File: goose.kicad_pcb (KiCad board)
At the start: 2 copper layers, 28 x 28 mm, 9 parts, among them J1 Conn_01x04, U1 AT42QT1011-TSHR

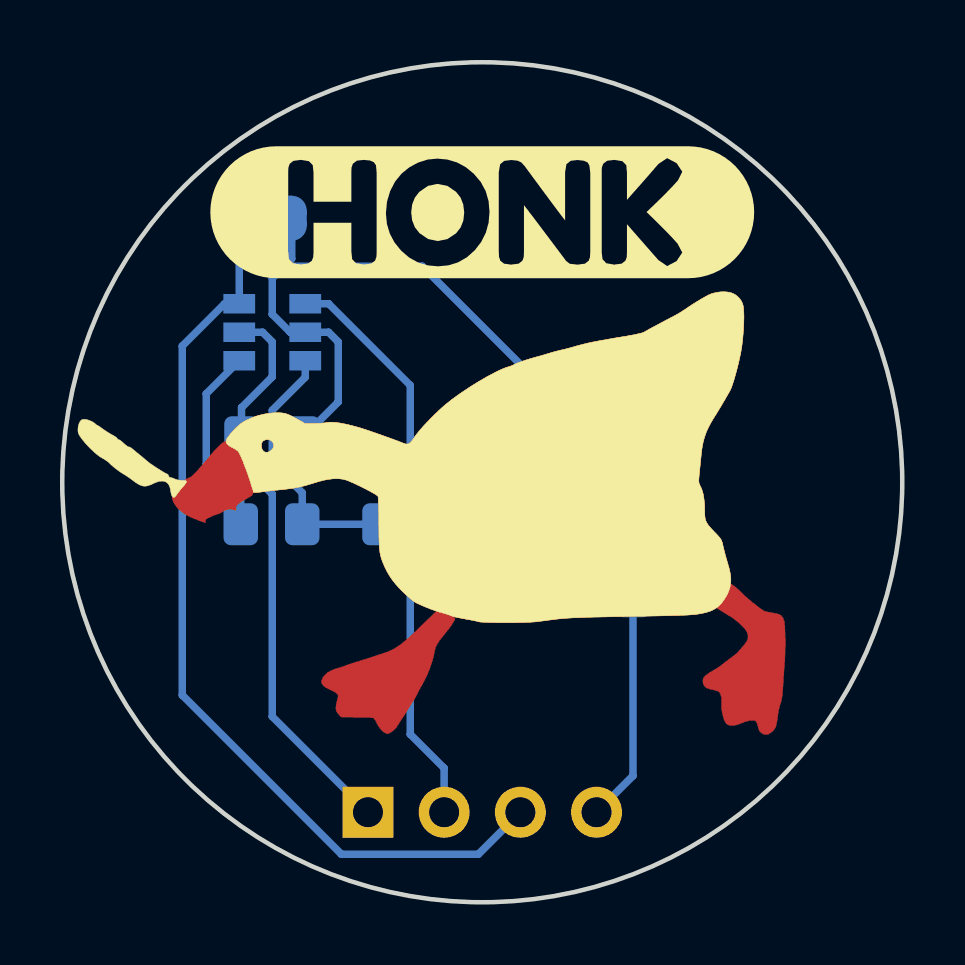
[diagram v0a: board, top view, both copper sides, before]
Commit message: Added a version that uses a chip that's actually in stock
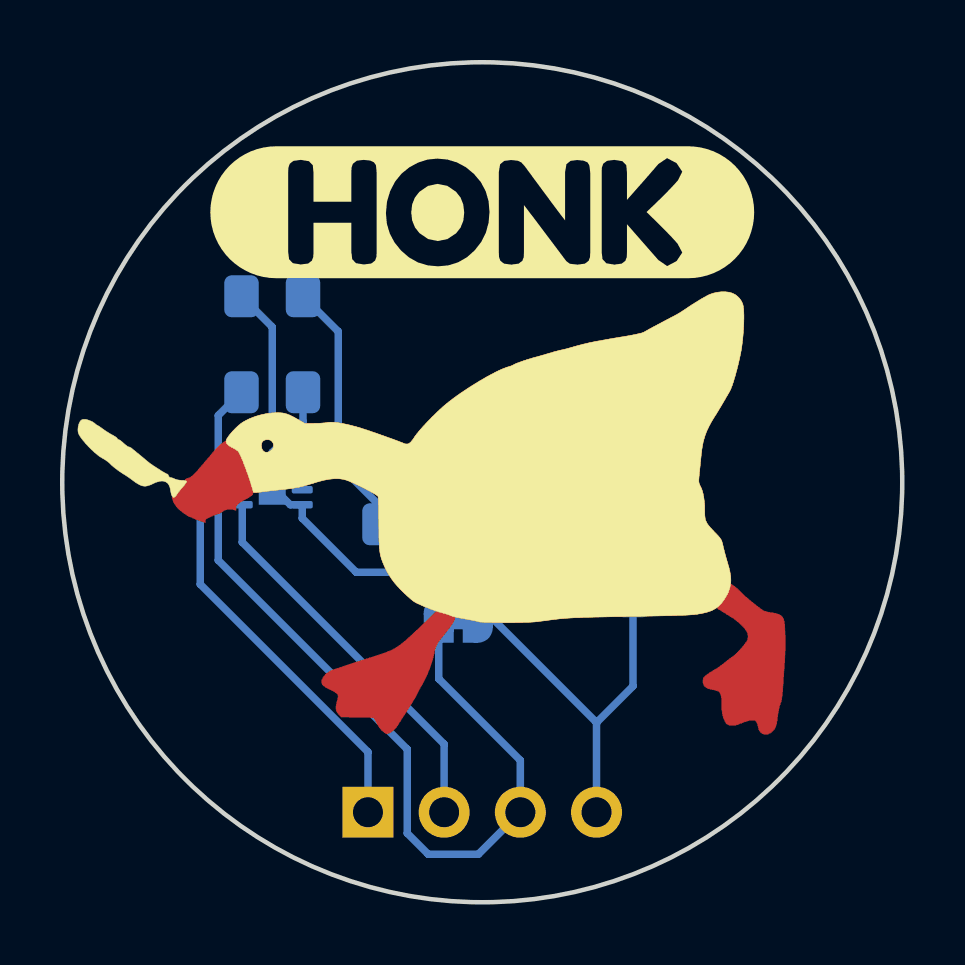
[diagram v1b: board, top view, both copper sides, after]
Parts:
- U1: value AT42QT1011-TSHR -> AT42QT1011-M; footprint Package_TO_SOT_SMD:SOT-23-6 -> Package_DFN_QFN:DFN-8-1EP_2x2mm_P0.5mm_EP0.9x1.5mm
- moved JP1 14.8 mm to (99.2, 104.6)
- moved C2 7.60 mm to (93.0, 93.8)
- moved U1 5.00 mm to (93.0, 100.0)
- moved C1 1.50 mm to (93.0, 97.0)
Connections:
- U1 pad 1: honk -> Net-(C2-Pad1)
- U1 pad 2: 0V -> (no net)
- U1 pad 3: Net-(C2-Pad1) -> (no net)
- U1 pad 4: Net-(C2-Pad2) -> 0V
- U1 pad 5: Vin -> honk
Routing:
- net 0V: track 35.9 -> 26.1 mm
- net honk: track 19.3 -> 13.0 mm
- net sync: track 31.2 -> 26.8 mm
- net Vin: track 19.1 -> 17.7 mm
- net Net-(C2-Pad1): track 8.99 -> 10.3 mm
